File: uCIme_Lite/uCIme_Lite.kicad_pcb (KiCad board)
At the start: 4 copper layers, 65 x 56 mm, 73 parts, among them J1 USB_MODE, J10 JACK_MODE, J11 SERIAL_MODE, J12 SERIAL_VOLTAGE_SELECT, J2 JACK_POWER_IN, J3 USB_POWER_IN, J4 USB_PC, J5 GPIO, J6 5V_ENABLE, J7 SERIAL, J8 JACK_POWER_OUT, J9 USB_POWER_OUT, Q1 BSS138, Q2 BUK7M27-80EX, Q3 BUK7M27-80EX, Q4 BSS138, Q5 BSS138, Q6 BSS138, Q7 BSS138, Q8 BSS138, U1 LM74502, U2 LM74502, U3 AP2204K-ADJ, U4 AP2204K-ADJ, U5 FT230XS, U6 TXB0104D

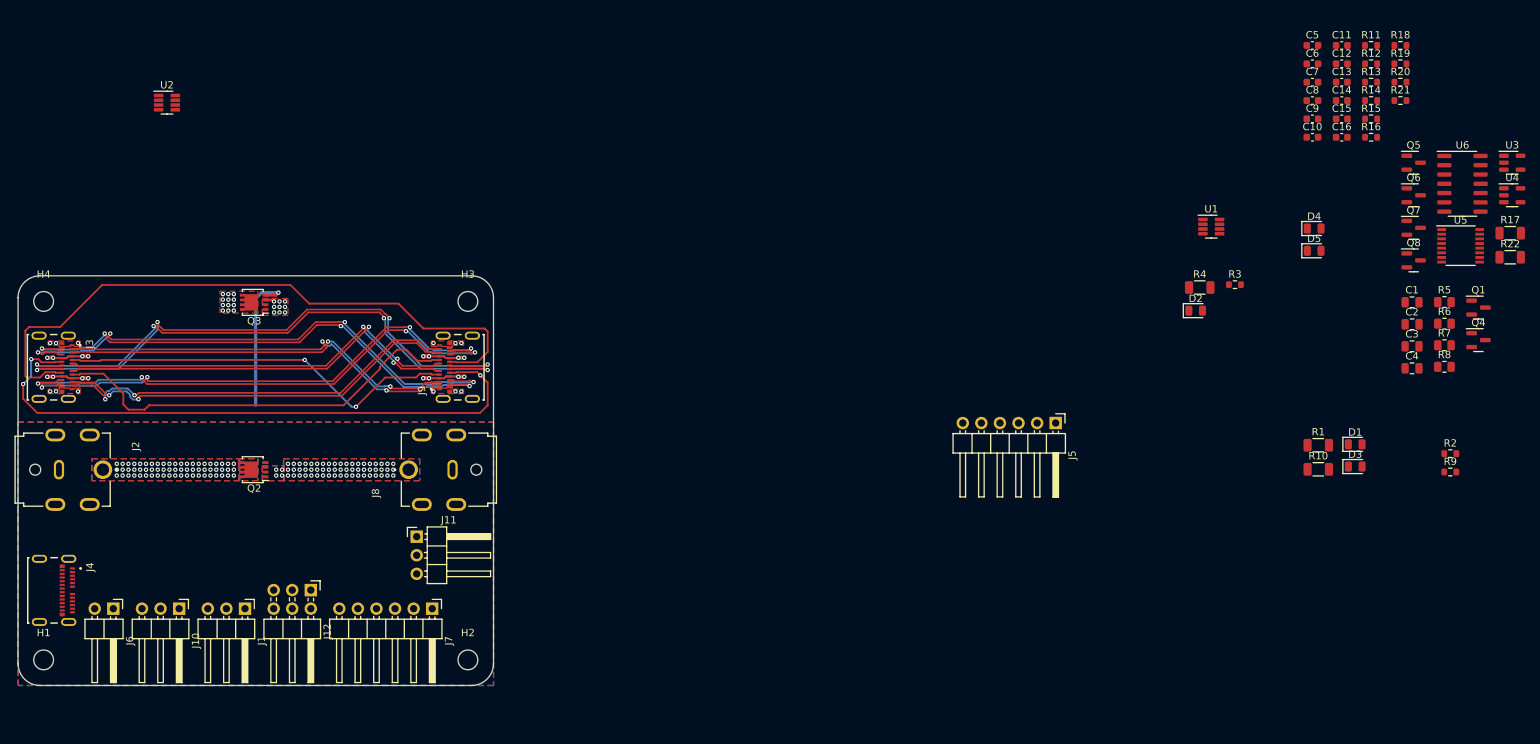
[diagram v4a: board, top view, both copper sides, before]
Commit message: lite: Routed FTDI USB-C connector.
Signed-off-by: Adrien Ricciardi <aricciardi@baylibre.com>
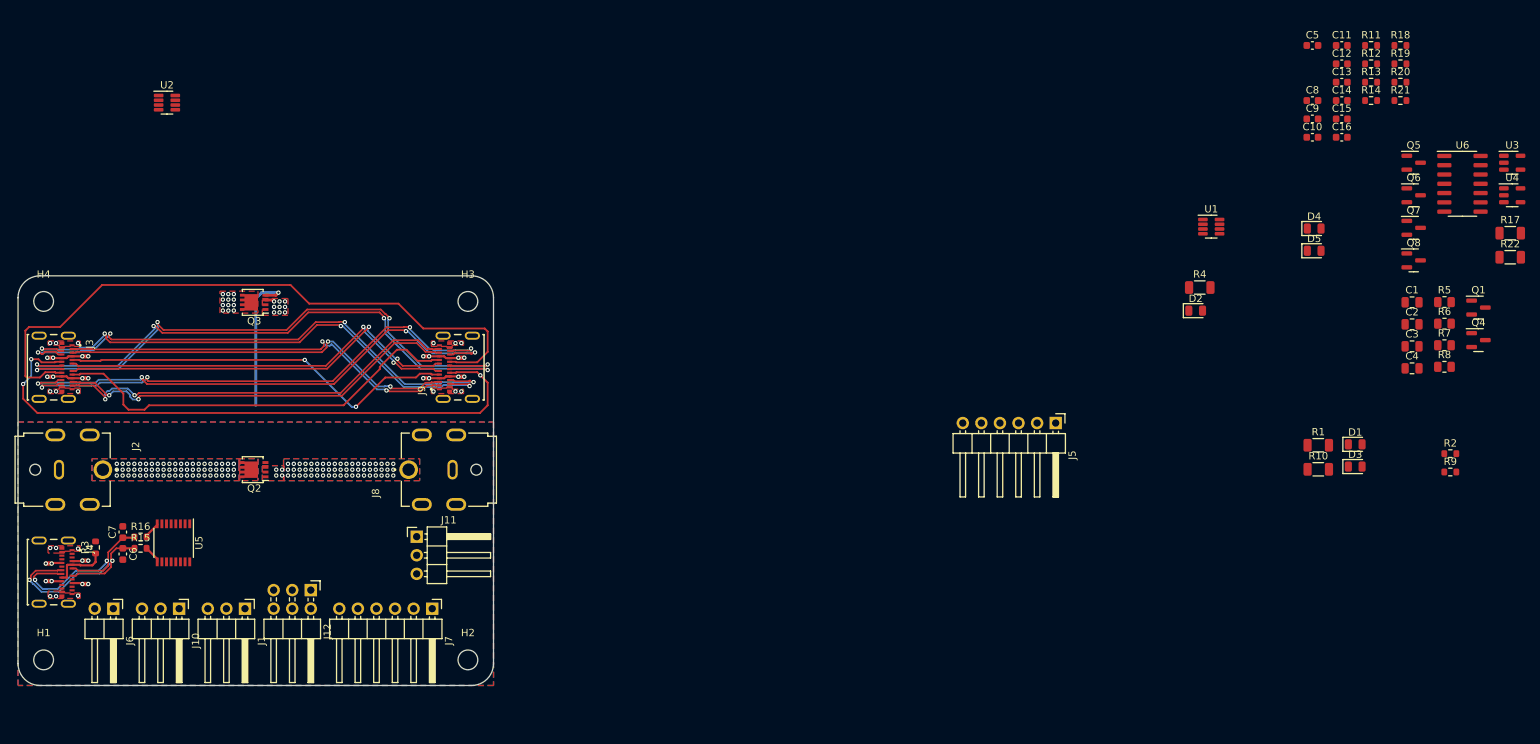
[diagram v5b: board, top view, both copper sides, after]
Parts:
- moved U5 180.6 mm to (86.2, 93.5), turned to -90 degrees
- moved R15 178.2 mm to (81.8, 94.2)
- moved R16 176.9 mm to (81.8, 92.7)
- moved C6 175.9 mm to (79.3, 95.0), turned to -90 degrees
- moved C7 173.9 mm to (79.3, 92.0), turned to 90 degrees
- moved R3 159.8 mm to (75.6, 94.1), turned to 90 degrees
- moved J4 2.50 mm to (68.5, 97.5)
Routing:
- net /D_N: track 0.00 -> 30.4 mm, vias 0 -> 2
- net /D_P: track 0.00 -> 28.5 mm, vias 0 -> 2
- net +5V: track 0.00 -> 8.92 mm, vias 0 -> 8
- net Net-(J4-CC1): track 0.00 -> 7.62 mm
- net Net-(U5-USBDM): track 0.00 -> 2.45 mm
- net Net-(U5-USBDP): track 0.00 -> 2.20 mm
- net GND: vias 12 -> 18
- added copper zone on In2.Cu, net +5V
- removed copper zone on In2.Cu, net GND

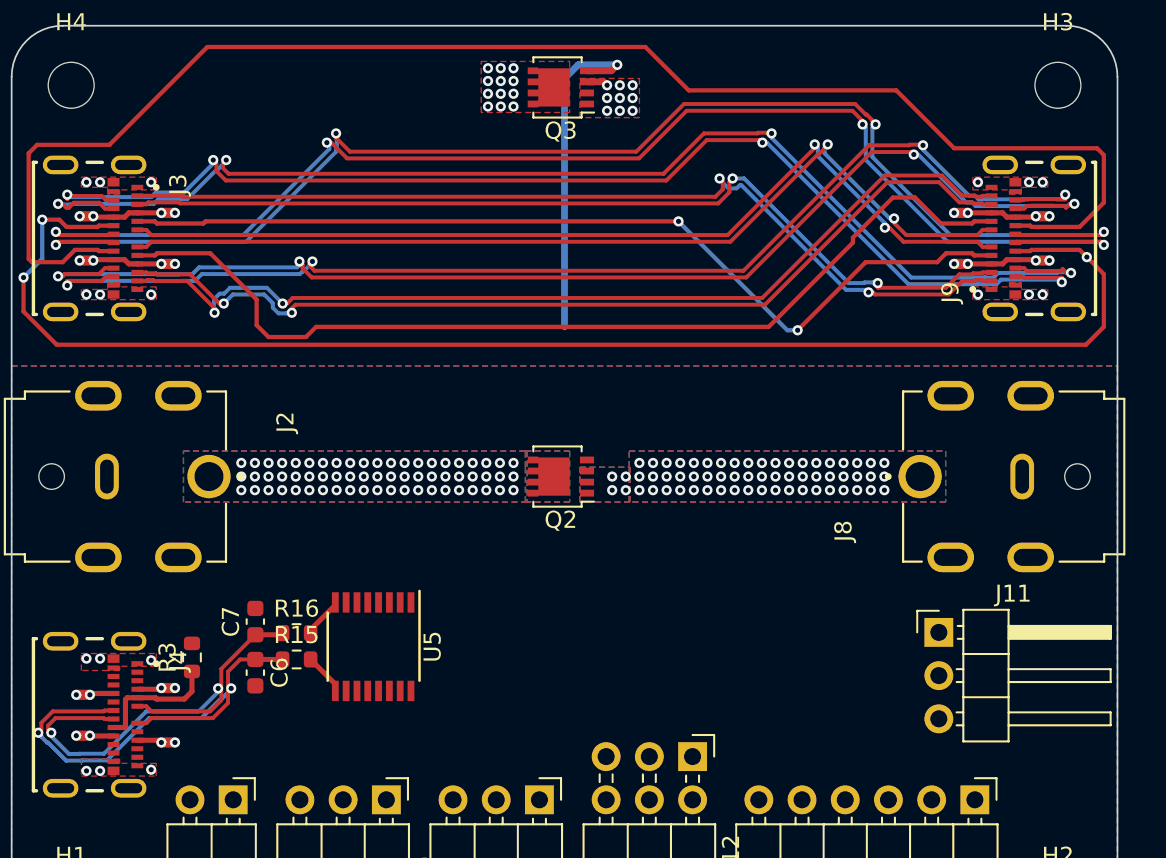
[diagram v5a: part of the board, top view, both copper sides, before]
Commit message: lite: Matched quite all USB connectors differential pair length.
Signed-off-by: Adrien Ricciardi <aricciardi@baylibre.com>
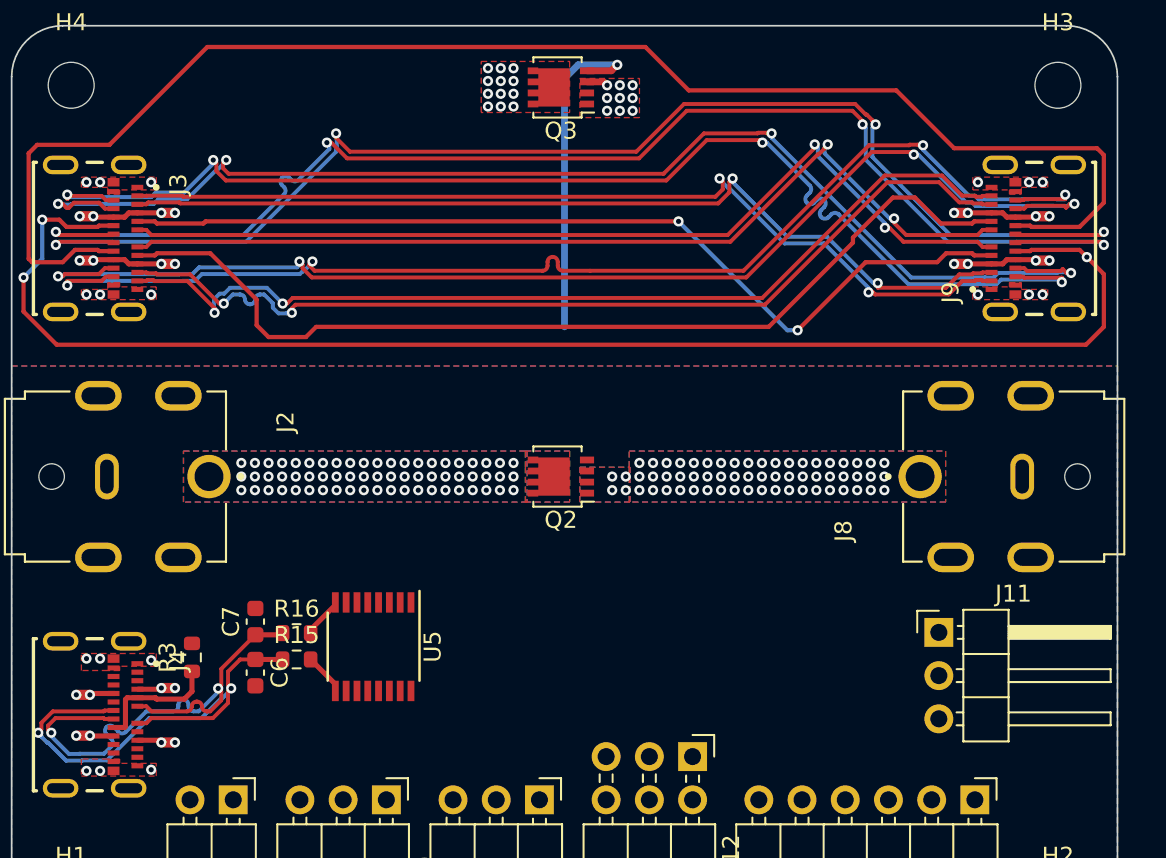
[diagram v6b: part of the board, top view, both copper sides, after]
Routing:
- net /D_P: track 28.5 -> 31.4 mm
- net /SSRX1_P: track 71.2 -> 73.4 mm
- net /SSTX2_P: track 71.2 -> 72.3 mm
- net /D2_N: track 79.2 -> 80.2 mm
- net /SSRX2_N: track 55.7 -> 56.3 mm

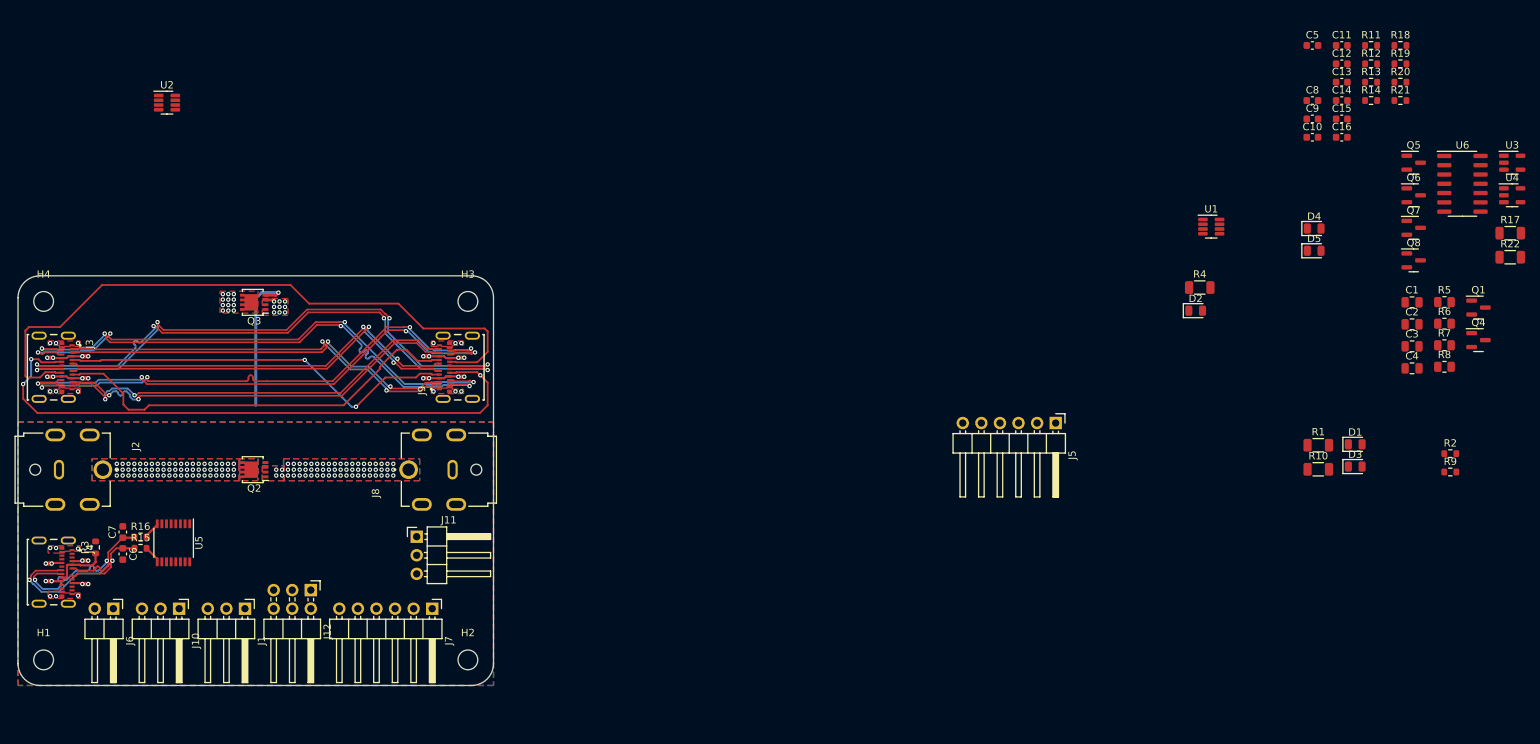
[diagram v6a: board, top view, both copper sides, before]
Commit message: lite: Updated serial and GPIO double-row pin header connector in PCB.
Also moved a bit the pin headers out of the PCB to make some room for the remaining components.

Signed-off-by: Adrien Ricciardi <aricciardi@baylibre.com>
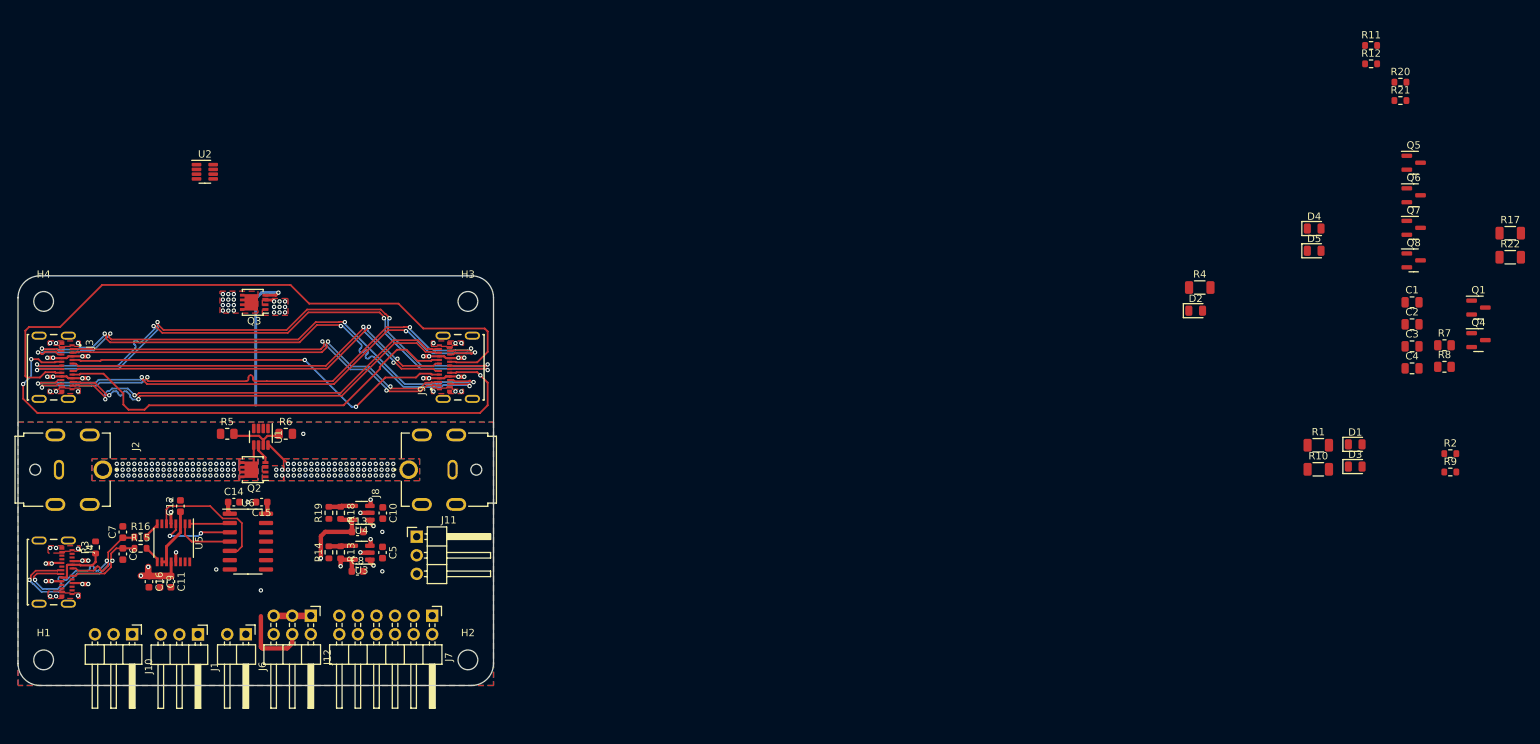
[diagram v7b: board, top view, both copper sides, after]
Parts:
- removed J5: GPIO, Connector_PinHeader_2.54mm:PinHeader_1x06_P2.54mm_Horizontal
- J7: value SERIAL -> SERIAL_AND_GPIO; footprint Connector_PinHeader_2.54mm:PinHeader_1x06_P2.54mm_Horizontal -> Connector_PinHeader_2.54mm:PinHeader_2x06_P2.54mm_Horizontal
- moved C11 176.0 mm to (85.9, 98.8), turned to -90 degrees
- moved C16 174.0 mm to (82.9, 98.8), turned to -90 degrees
- moved U6 173.1 mm to (96.4, 93.3)
- moved C12 169.9 mm to (87.2, 88.5), turned to 90 degrees
- moved C9 169.8 mm to (84.4, 98.8), turned to -90 degrees
- moved R5 167.4 mm to (93.6, 78.6)
- moved U3 166.1 mm to (112.0, 94.8), turned to 180 degrees
- moved U4 163.2 mm to (112.0, 89.4), turned to 180 degrees
- moved C14 161.1 mm to (94.5, 87.9)
- moved R6 159.1 mm to (101.6, 78.6)
- moved R19 158.8 mm to (107.5, 89.4), turned to 90 degrees
- moved R18 158.3 mm to (109.1, 89.4), turned to -90 degrees
- moved C15 156.7 mm to (98.3, 87.9), turned to 180 degrees
- moved R14 155.3 mm to (107.5, 94.8), turned to 90 degrees
- moved R13 154.8 mm to (109.1, 94.8), turned to -90 degrees
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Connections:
- J7 pad 2: /Controller//SERIAL_CTS -> GND
- J7 pad 3: Net-(J6-Pin_1) -> /Controller//SERIAL_CTS
- J7 pad 4: /Controller/SERIAL_TX -> /Controller/GPIO_0
- J7 pad 5: /Controller/SERIAL_RX -> Net-(J6-Pin_1)
- J7 pad 6: /Controller//SERIAL_RTS -> +5V
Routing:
- net +3.3V: track 0.00 -> 31.7 mm, vias 0 -> 2
- net Net-(U5-~{CTS}): track 0.00 -> 18.5 mm
- net +1V8: track 0.00 -> 12.7 mm, vias 0 -> 1
- net +5V: track 8.92 -> 20.2 mm, vias 8 -> 14
- net /Controller/UART_RX: track 0.00 -> 10.4 mm, vias 0 -> 2
- net +3.3VA: track 0.00 -> 9.95 mm
- net Net-(U5-~{RTS}): track 0.00 -> 8.01 mm
- net Net-(U1-OV): track 0.00 -> 7.57 mm
- net Net-(J12-Pin_1): track 0.00 -> 6.73 mm
- net GND: track 0.00 -> 5.55 mm, vias 18 -> 28
- net /Controller/UART_TX: track 0.00 -> 5.52 mm
- net /Power Management/OUTPUT_JACK_V+: track 0.00 -> 3.79 mm
- net /Power Management/INPUT_JACK_V+: track 0.00 -> 3.51 mm
- net Net-(U4-ADJ): track 0.00 -> 3.38 mm
- net Net-(U3-ADJ): track 0.00 -> 3.36 mm
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
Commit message: lite: Routed jack power channel gate driver.
Signed-off-by: Adrien Ricciardi <aricciardi@baylibre.com>
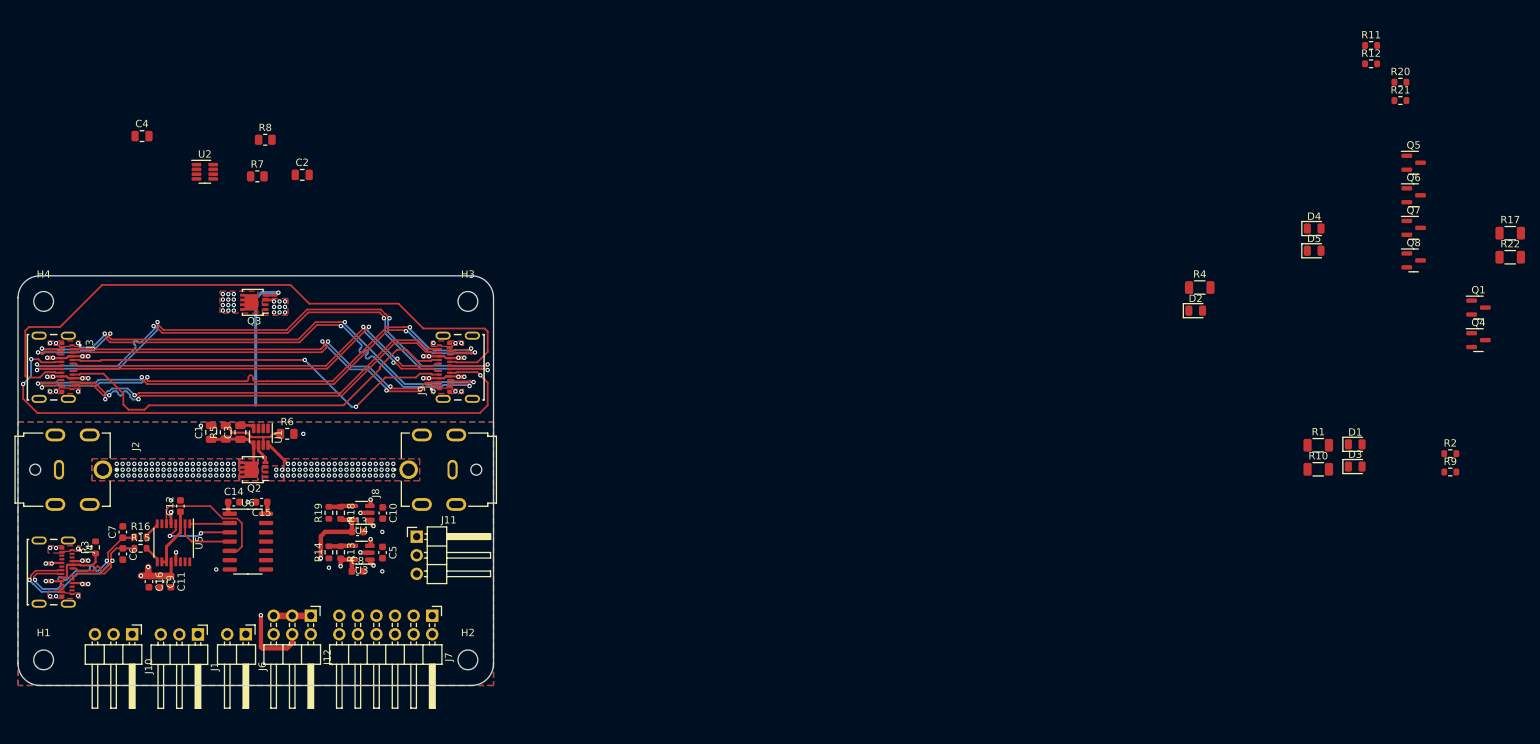
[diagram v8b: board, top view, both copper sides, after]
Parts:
- moved C4 176.5 mm to (82.0, 37.9)
- moved C1 165.1 mm to (91.4, 78.4), turned to 90 degrees
- moved R8 164.2 mm to (98.8, 38.4)
- moved R7 163.9 mm to (97.7, 43.4)
- moved C3 160.6 mm to (95.4, 78.4), turned to 90 degrees
- moved C2 153.1 mm to (103.8, 43.2)
- moved R5 0.28 mm to (93.4, 78.4), turned to 90 degrees
- moved R6 0.20 mm to (101.8, 78.6)
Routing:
- net /Power Management/INPUT_JACK_V+: track 3.51 -> 9.69 mm
- net +3.3V: track 31.7 -> 35.2 mm
- net Net-(U1-OV): track 7.57 -> 9.83 mm
- net Net-(U1-VCAP): track 0.00 -> 2.00 mm
- net GND: vias 28 -> 30
